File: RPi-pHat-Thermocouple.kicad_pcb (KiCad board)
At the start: 2 copper layers, 65 x 30 mm, 36 parts, among them J1 RPi_GPIO, P1 CONN_01X02, P2 CONN_01X02, P3 CONN_01X02, P4 CONN_01X02, P6 CONN_01X03, Q1 NUD3124, SW1 Write, U1 MAX31850K, U2 DS18S20, U3 MAX31850K, U4 MAX31850K, U5 AT24CS32, U6 MAX31850K

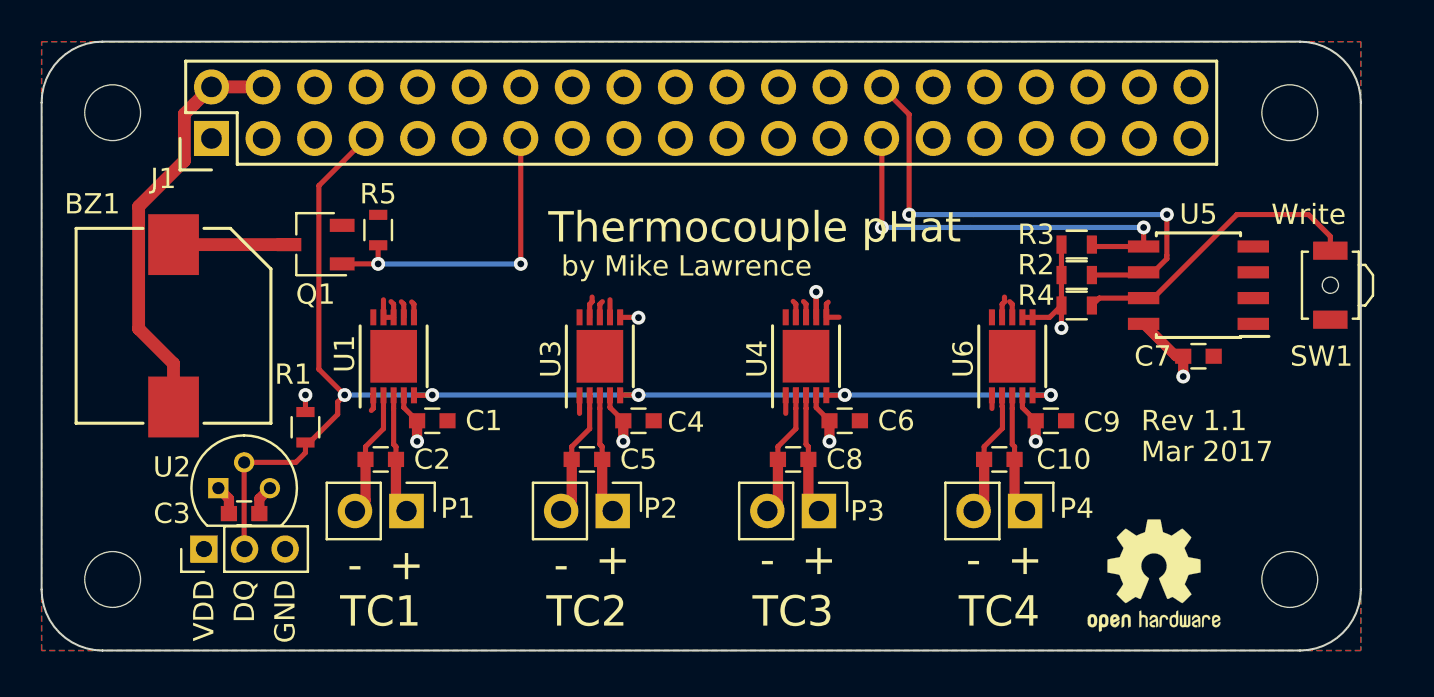
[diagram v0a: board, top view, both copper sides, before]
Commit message: Added Analog Power Supply
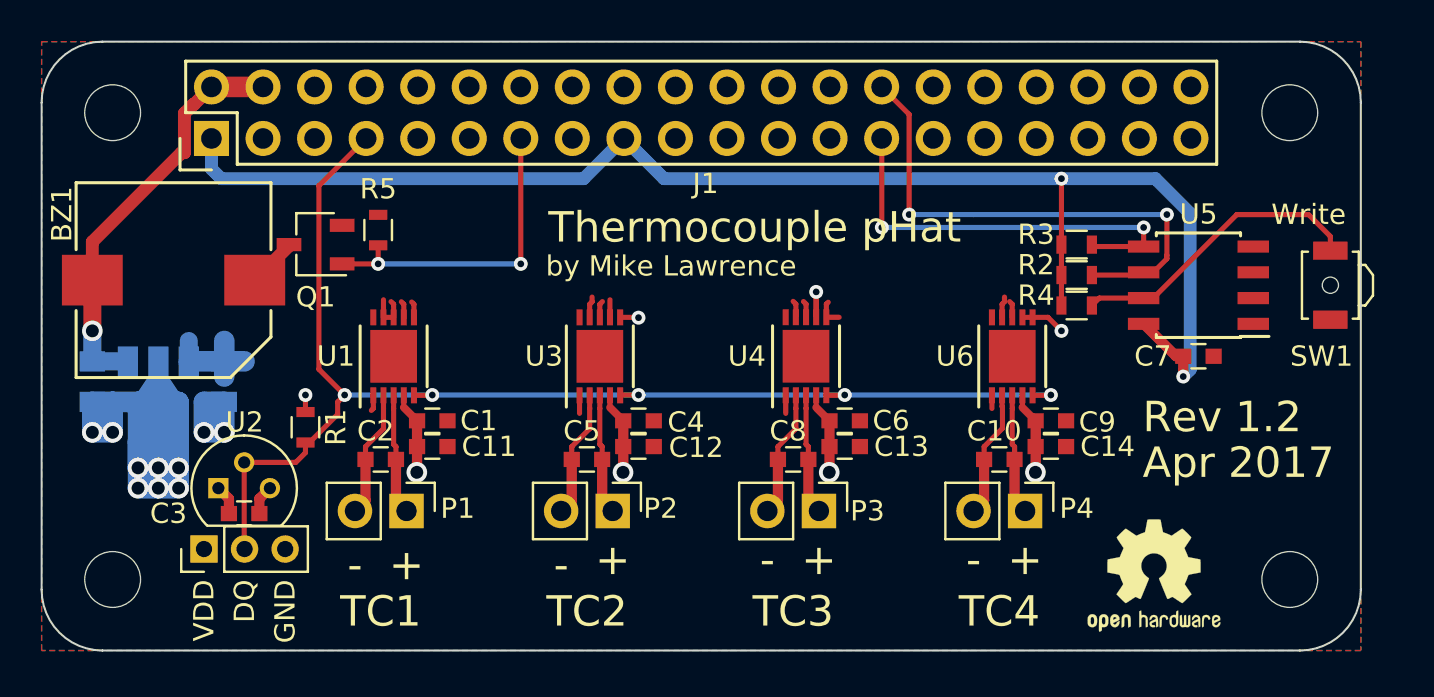
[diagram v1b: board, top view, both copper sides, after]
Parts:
- removed the REF*** at (19.1, 37.5)
- added C11: 10nF, Capacitors_SMD:C_0603, F.Cu at (31.8, 44.5)
- added C12: 10nF, Capacitors_SMD:C_0603, F.Cu at (41.9, 44.5)
- added C13: 10nF, Capacitors_SMD:C_0603, F.Cu at (52.1, 44.5)
- added C14: 10nF, Capacitors_SMD:C_0603, F.Cu at (62.2, 44.5)
- added C15: 2.2uF, Capacitors_SMD:C_0805, B.Cu at (21.5, 41.2)
- added C16: 2.2uF, Capacitors_SMD:C_0805, B.Cu at (15.0, 41.2)
- added REF***: OSHW-Logo2_7.3x6mm_SilkScreen, Symbols:OSHW-Logo2_7.3x6mm_SilkScreen, B.Cu at (67.3, 50.8)
- added U7: MCP1754ST, TO_SOT_Packages_SMD:SOT89-3_Housing, B.Cu at (18.2, 41.8)
- moved BZ1 2.25 mm to (19.0, 36.2), turned to 0 degrees
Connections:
- C1 pad 2: +3V3 -> +3.3VA
- C3 pad 2: +3V3 -> +3.3VA
- C4 pad 2: +3V3 -> +3.3VA
- C6 pad 2: +3V3 -> +3.3VA
- C9 pad 2: +3V3 -> +3.3VA
- P6 pad 1: +3V3 -> +3.3VA
- R1 pad 2: +3V3 -> +3.3VA
- U1 pad 11: Net-(U1-Pad11) -> GND
- U1 pad 4: +3V3 -> +3.3VA
- U2 pad 3: +3V3 -> +3.3VA
- U3 pad 11: Net-(U3-Pad11) -> GND
- U3 pad 4: +3V3 -> +3.3VA
- U3 pad 6: +3V3 -> +3.3VA
- U4 pad 11: Net-(U4-Pad11) -> GND
- U4 pad 4: +3V3 -> +3.3VA
- U4 pad 7: +3V3 -> +3.3VA
- U6 pad 11: Net-(U6-Pad11) -> GND
- U6 pad 4: +3V3 -> +3.3VA
- U6 pad 6: +3V3 -> +3.3VA
- U6 pad 7: +3V3 -> +3.3VA
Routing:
- net +3V3: track 25.7 -> 70.3 mm, vias 9 -> 2
- net GND: track 16.2 -> 54.4 mm, vias 0 -> 10
- net +3.3VA: track 0.00 -> 30.1 mm, vias 0 -> 8
- net Net-(U1-Pad11): track 3.60 -> 0.00 mm
- net Net-(U6-Pad11): track 3.60 -> 0.00 mm
- net Net-(U3-Pad11): track 3.60 -> 0.00 mm
- net Net-(U4-Pad11): track 3.60 -> 0.00 mm
- net Net-(BZ1-Pad2): track 5.69 -> 2.45 mm
- net +5V: track 20.5 -> 20.4 mm, vias 0 -> 1
- added copper zone on B.Cu, net +3.3VA
- removed copper zone on B.Cu, net +3V3
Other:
- board text added: "Apr 2017"
- board text added: "Rev 1.2"
- board text removed: "Mar 2017"
- board text removed: "Rev 1.1"

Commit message: Remove one MAX38150K add switching power supply
Removed one MAX38150K so now there are three on the board.
Added switching power supply to safely backpower the Raspberry Pi Zero.
Now has Barrel Jack for input power.
Updated schematic BOM fields and added KiBOM support.
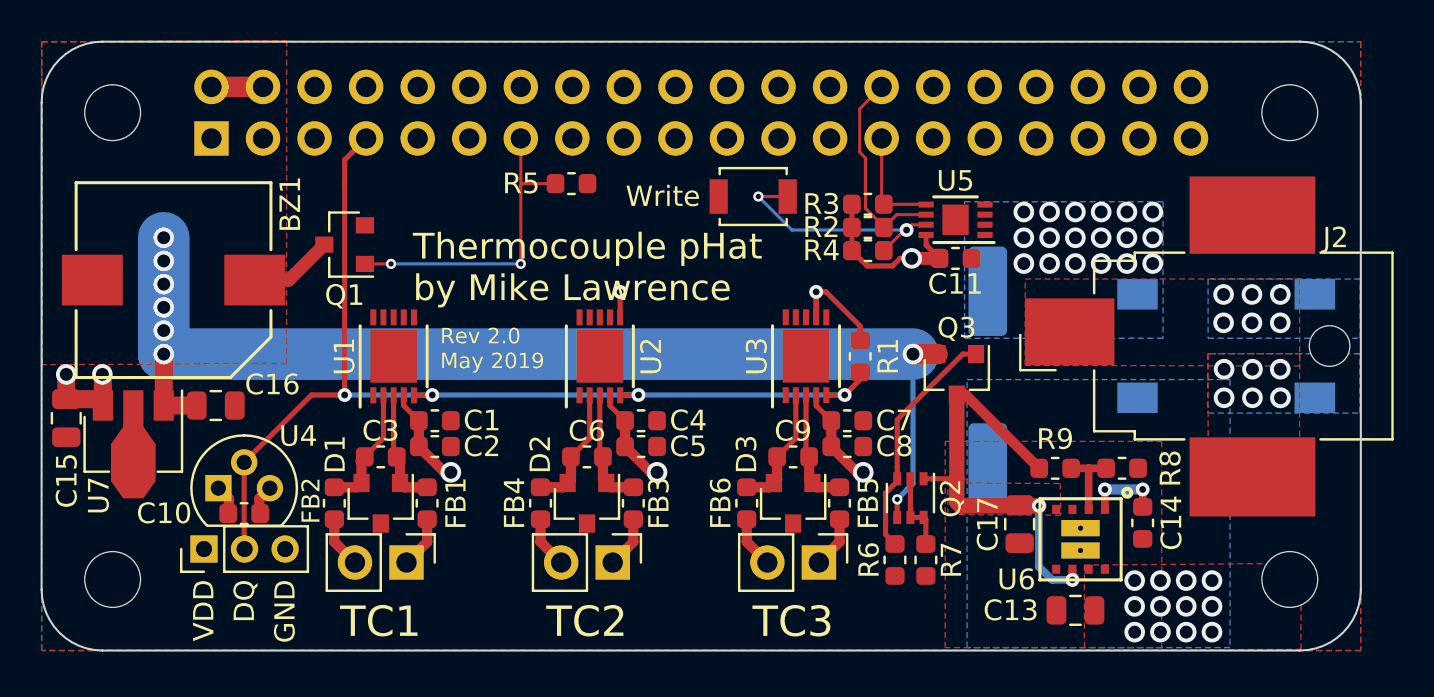
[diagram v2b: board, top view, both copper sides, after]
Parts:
- removed P4: CONN_01X02, Pin_Headers:Pin_Header_Straight_1x02_Pitch2.54mm
- removed the REF*** at (67.3, 50.8)
- added C17: 22uF, Capacitor_SMD:C_0805_2012Metric, F.Cu at (60.7, 48.3)
- added D1: NUP2105LT1G, Package_TO_SOT_SMD:SOT-23, F.Cu at (29.2, 47.2)
- added D2: NUP2105LT1G, Package_TO_SOT_SMD:SOT-23, F.Cu at (39.4, 47.2)
- added D3: NUP2105LT1G, Package_TO_SOT_SMD:SOT-23, F.Cu at (49.5, 47.2)
- added D4: D_Bridge_+-AA, Diode_SMD:Diode_Bridge_Vishay_DFS, B.Cu at (70.9, 39.5)
- added FB1: 1k, Inductor_SMD:L_0603_1608Metric, F.Cu at (31.5, 47.2)
- added FB2: 1k, Inductor_SMD:L_0603_1608Metric, F.Cu at (26.9, 47.2)
- added FB3: 1k, Inductor_SMD:L_0603_1608Metric, F.Cu at (41.7, 47.2)
- added FB4: 1k, Inductor_SMD:L_0603_1608Metric, F.Cu at (37.1, 47.2)
- added FB5: 1k, Inductor_SMD:L_0603_1608Metric, F.Cu at (51.8, 47.2)
- added FB6: 1k, Inductor_SMD:L_0603_1608Metric, F.Cu at (47.2, 47.2)
- added J2: Barrel_Jack_Switch, Connector_BarrelJack:BarrelJack_CUI_PJ-036AH-SMT_Horizontal, F.Cu at (69.0, 39.5)
- added Q2: BCM857BS, Package_TO_SOT_SMD:SOT-363_SC-70-6, F.Cu at (55.3, 47.0)
- added Q3: DMG2305UX, Package_TO_SOT_SMD:SOT-23, F.Cu at (57.6, 40.9)
- added R6: 47k, Resistor_SMD:R_0603_1608Metric, F.Cu at (54.5, 50.0)
- added R7: 10k, Resistor_SMD:R_0603_1608Metric, F.Cu at (56.1, 50.0)
- added R8: 44.2k, Resistor_SMD:R_0603_1608Metric, F.Cu at (65.7, 45.5)
- added R9: 232k, Resistor_SMD:R_0603_1608Metric, F.Cu at (62.4, 45.5)
- BZ1: footprint cui-ml:CMI-9655S-SMT -> Buzzer_Beeper-ML:MagneticBuzzer_CUI-CMI-9655S
- C1, C2, C3, C4, C5, C6, C7, C8, C9: footprint Capacitors_SMD:C_0603 -> Capacitor_SMD:C_0603_1608Metric
- C10, C11: value 10nF -> 0.1uF; footprint Capacitors_SMD:C_0603 -> Capacitor_SMD:C_0603_1608Metric
- C12: value 10nF -> 330uF; footprint Capacitors_SMD:C_0603 -> Capacitor_SMD:CP_Elec_10x7.9; moved to B.Cu
- C13: value 10nF -> 22uF; footprint Capacitors_SMD:C_0603 -> Capacitor_SMD:C_0805_2012Metric
- C14: value 10nF -> 3.3nF; footprint Capacitors_SMD:C_0603 -> Capacitor_SMD:C_0603_1608Metric
- C15, C16: footprint Capacitors_SMD:C_0805 -> Capacitor_SMD:C_0805_2012Metric; moved to F.Cu
- J1: footprint raspberry-ml:Pin_Header_Straight_2x20 -> Connector_PinSocket_2.54mm:PinSocket_2x20_P2.54mm_Vertical; moved to B.Cu
- Q1: footprint TO_SOT_Packages_SMD:TSOT-23 -> Package_TO_SOT_SMD:SOT-23
- R1, R2, R3, R4, R5: footprint Resistors_SMD:R_0603 -> Resistor_SMD:R_0603_1608Metric
- SW1: footprint Buttons_Switches_SMD:SW_SPST_B3U-3000P-B -> Button_Switch_SMD:SW_SPST_B3U-1000P
- U1, U3: footprint Housings_DFN_QFN_ML:TDFN-10-1EP_3x4mm_Pitch0.5mm -> Package_DFN_QFN-ML:TDFN-10-1EP_3x4mm_Pitch0.5mm
- U2: value DS18S20 -> MAX31850K; footprint TO_SOT_Packages_THT:TO-92_Molded_Narrow -> Package_DFN_QFN-ML:TDFN-10-1EP_3x4mm_Pitch0.5mm
- U4: value MAX31850K -> DS18S20; footprint Housings_DFN_QFN_ML:TDFN-10-1EP_3x4mm_Pitch0.5mm -> Package_TO_SOT_THT:TO-92
- U5: footprint Housings_SOIC:SOIC-8_3.9x4.9mm_Pitch1.27mm -> Package_DFN_QFN:DFN-8-1EP_3x2mm_P0.5mm_EP1.3x1.5mm
- U6: value MAX31850K -> LMZ21700; footprint Housings_DFN_QFN_ML:TDFN-10-1EP_3x4mm_Pitch0.5mm -> Converter_DCDC-ML:Converter_DCDC_Texas-SIL0008E
- U7: footprint TO_SOT_Packages_SMD:SOT89-3_Housing -> Package_TO_SOT_SMD:SOT-89-3; moved to F.Cu
- moved REF*** 45.8 mm to (22.5, 41.0)
- moved C10 37.3 mm to (22.5, 47.8)
- moved U4 29.7 mm to (21.2, 46.5), turned to 0 degrees
- moved SW1 28.8 mm to (47.6, 32.1), turned to 0 degrees
- moved R1 27.6 mm to (52.8, 40.0)
- moved C11 27.4 mm to (57.5, 35.2)
- moved J1 24.2 mm to (20.9, 29.3), turned to 270 degrees
- moved U2 19.9 mm to (40.0, 40.0), turned to 90 degrees
- moved C7 17.6 mm to (52.2, 43.2), turned to 180 degrees
- moved C12 17.5 mm to (59.1, 41.1), turned to 90 degrees
- moved C13 13.9 mm to (63.4, 52.5), turned to 180 degrees
- moved C6 12.8 mm to (39.4, 45.0)
- moved C9 12.8 mm to (49.5, 45.0)
- moved U5 12.4 mm to (57.5, 33.3)
- moved R4 10.6 mm to (53.2, 34.8)
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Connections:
- C10 pad 1: /TC4+ -> +3.3VA
- C10 pad 2: /TC4- -> GND
- C12 pad 1: +3.3VA -> /VBulk
- C13 pad 1: +3.3VA -> /VBulk
- C14 pad 1: +3.3VA -> Net-(C14-Pad1)
- C2 pad 1: /TC1+ -> +3.3VA
- C2 pad 2: /TC1- -> GND
- C3 pad 1: GND -> Net-(C3-Pad1)
- C3 pad 2: +3.3VA -> Net-(C3-Pad2)
- C5 pad 1: /TC2+ -> +3.3VA
- C5 pad 2: /TC2- -> GND
- C6 pad 1: GND -> Net-(C6-Pad1)
- C6 pad 2: +3.3VA -> Net-(C6-Pad2)
- C7 pad 1: +3V3 -> GND
- C7 pad 2: GND -> +3.3VA
- C8 pad 1: /TC3+ -> +3.3VA
- C8 pad 2: /TC3- -> GND
- C9 pad 1: GND -> Net-(C9-Pad1)
- C9 pad 2: +3.3VA -> Net-(C9-Pad2)
- J1 pad 1: +3V3 -> (no net)
- J1 pad 10: Net-(J1-Pad10) -> (no net)
- J1 pad 11: Net-(J1-Pad11) -> (no net)
- J1 pad 12: Net-(J1-Pad12) -> (no net)
- J1 pad 15: Net-(J1-Pad15) -> (no net)
- J1 pad 16: Net-(J1-Pad16) -> (no net)
- J1 pad 17: +3V3 -> (no net)
- J1 pad 18: Net-(J1-Pad18) -> (no net)
- J1 pad 19: Net-(J1-Pad19) -> (no net)
- J1 pad 21: Net-(J1-Pad21) -> (no net)
- J1 pad 22: Net-(J1-Pad22) -> (no net)
- J1 pad 23: Net-(J1-Pad23) -> (no net)
- J1 pad 24: Net-(J1-Pad24) -> (no net)
- J1 pad 26: Net-(J1-Pad26) -> (no net)
- J1 pad 29: Net-(J1-Pad29) -> (no net)
- J1 pad 3: Net-(J1-Pad3) -> (no net)
- J1 pad 31: Net-(J1-Pad31) -> (no net)
- J1 pad 32: Net-(J1-Pad32) -> (no net)
- J1 pad 33: Net-(J1-Pad33) -> (no net)
- J1 pad 35: Net-(J1-Pad35) -> (no net)
- J1 pad 36: Net-(J1-Pad36) -> (no net)
- J1 pad 37: Net-(J1-Pad37) -> (no net)
- J1 pad 38: Net-(J1-Pad38) -> (no net)
- J1 pad 40: Net-(J1-Pad40) -> (no net)
- J1 pad 5: Net-(J1-Pad5) -> (no net)
- J1 pad 8: Net-(J1-Pad8) -> (no net)
- R2 pad 1: +3V3 -> +3.3VA
- R3 pad 1: +3V3 -> +3.3VA
- R4 pad 1: +3V3 -> +3.3VA
- SW1 pad 1: Net-(R4-Pad2) -> GND
- SW1 pad 2: GND -> Net-(R4-Pad2)
- U1 pad 2: /TC1- -> Net-(C3-Pad2)
- U1 pad 3: /TC1+ -> Net-(C3-Pad1)
- U2 pad 2: /W1 -> Net-(C6-Pad2)
- U2 pad 3: +3.3VA -> Net-(C6-Pad1)
- U3 pad 2: /TC2- -> Net-(C9-Pad2)
- U3 pad 3: /TC2+ -> Net-(C9-Pad1)
- U3 pad 6: +3.3VA -> GND
- U3 pad 7: GND -> +3.3VA
- U4 pad 2: /TC3- -> /W1
- U4 pad 3: /TC3+ -> +3.3VA
- U5 pad 8: +3V3 -> +3.3VA
- U6 pad 1: GND -> Net-(C14-Pad1)
- U6 pad 10: (no net) -> GND
- U6 pad 2: /TC4- -> Net-(R8-Pad1)
- U6 pad 3: /TC4+ -> (no net)
- U6 pad 4: +3.3VA -> /+5VB
- U6 pad 5: /W1 -> GND
- U6 pad 6: +3.3VA -> /+5VB
- U6 pad 7: +3.3VA -> /VBulk
- U6 pad 8: GND -> /VBulk
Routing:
- net +3V3: track 70.3 -> 0.00 mm, vias 2 -> 0
- net GND: track 54.4 -> 1.47 mm, vias 10 -> 18
- net +5V: track 20.4 -> 59.2 mm, vias 1 -> 8
- net /+5VB: track 0.00 -> 22.1 mm, vias 0 -> 2
- net /ID_SD: track 21.1 -> 5.41 mm, vias 2 -> 0
- net /ID_SC: track 25.8 -> 10.2 mm, vias 2 -> 0
- net Net-(Q2-Pad3): track 0.00 -> 11.8 mm
- net /W1: track 63.8 -> 52.5 mm, vias 5 -> 4
- net Net-(C3-Pad2): track 0.00 -> 6.54 mm
- net +3.3VA: track 30.1 -> 36.7 mm
- net /TC4-: track 6.30 -> 0.00 mm
- net Net-(C9-Pad2): track 0.00 -> 6.22 mm
- net Net-(C6-Pad2): track 0.00 -> 6.22 mm
- net Net-(C3-Pad1): track 0.00 -> 6.03 mm
- net /TC4+: track 5.96 -> 0.00 mm
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- added copper zone on F.Cu, net +5V
- added copper zone on F.Cu, net /+5VB
- added copper zone on B.Cu, net /AC1
- added copper zone on F.Cu, net /AC1
- added copper zone on B.Cu, net /AC2
- added copper zone on F.Cu, net /AC2
- added copper zone on B.Cu, net /VBulk
- added copper zone on F.Cu, net /VBulk
- added copper zone on B.Cu, net GND
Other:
- net class Default: via_dia 0.6858 -> 0.508; via_drill 0.3302 -> 0.254
- net class Power added: clearance 0.1524, trace_width 0.381, via_dia 1.016, via_drill 0.635
- rule pad_to_mask_clearance: 0 -> 0.0508
- rule via_min_drill: 0.3302 -> 0.254
- rule via_min_size: 0.6858 -> 0.508
- board text added: "Rev 2.0 May 2019"
- board text added: "Thermocouple pHat by Mike Lawrence"
- board text removed: "+"
- board text removed: "-"
- board text removed: "Apr 2017"
- board text removed: "Rev 1.2"
- board text removed: "TC4"
- board text removed: "Thermocouple pHat"
- board text removed: "Write"
- board text removed: "by Mike Lawrence"
